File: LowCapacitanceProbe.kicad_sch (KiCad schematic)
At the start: 39 parts, among them J1 u.Fl, J2 SMA, Q1 BF998, U2 SPX3819M5-L-5-0

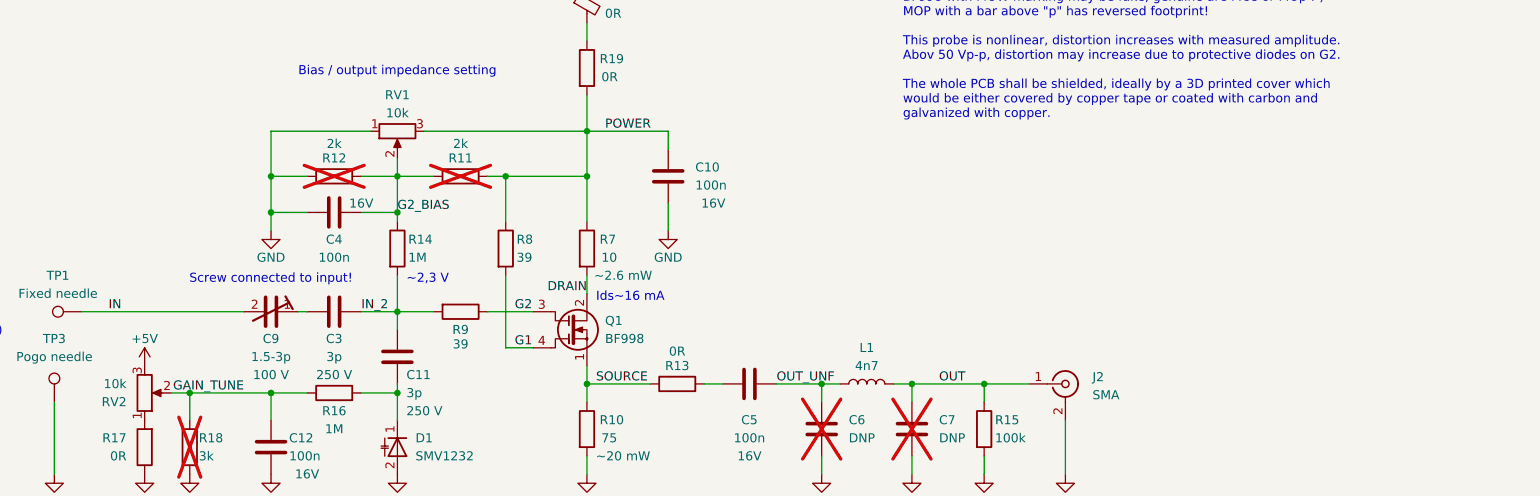
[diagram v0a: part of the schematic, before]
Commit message: Slight fixes, simulation modified for varicap analysis and noise analysis, started routing of PCB.
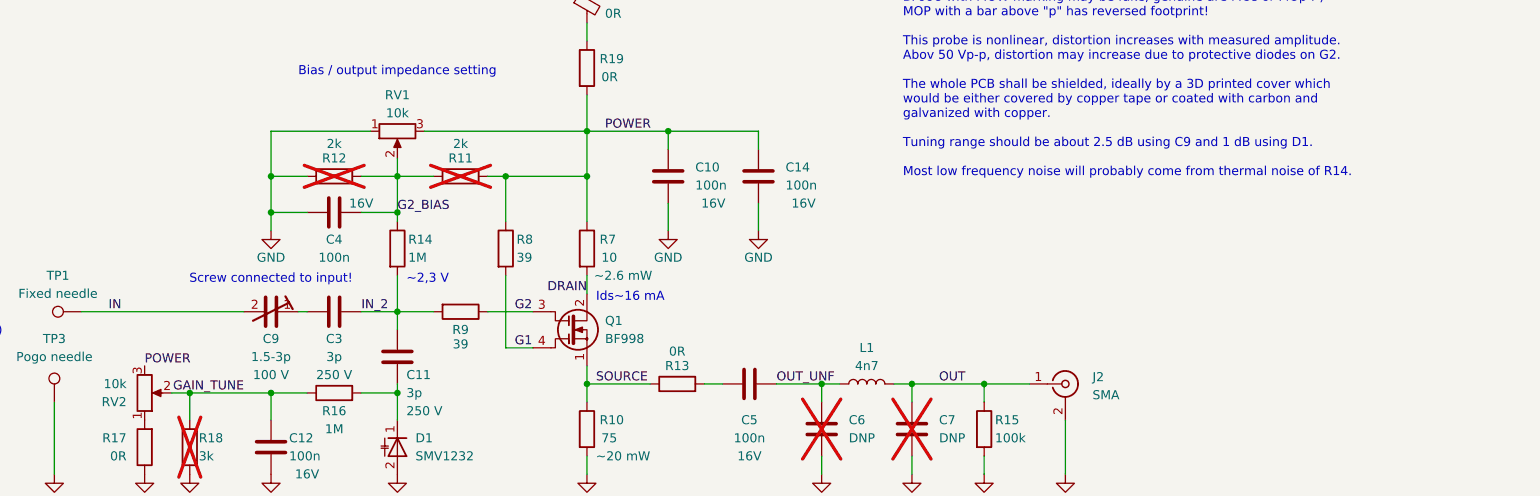
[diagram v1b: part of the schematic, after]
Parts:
- added C14: 100n, Capacitor_SMD:C_0402_1005Metric_Pad0.74x0.62mm_HandSolder, symbol Device:C
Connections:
- net +5V: no longer RV2.3
- net GND: now also C14.1
- net POWER: now also RV2.3, C14.2
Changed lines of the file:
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@@
 		)
 	)
-	(text "Calibration process:\n1) Perform this calibration in ESD safe environment!\n   Short the input, power up the probe (with VNA disconnected).\n   Not shorting the input may affect the measurement.\n2) Connect VNA, measure output impedance of the probe.\n   Tune the bias on gate 2 to get 50 Ohm output.\n3) Disconnect VNA, reconnect it to measure S21 of the probe.\n   (If varicap tuning is assembled, set it to highest possible voltage.)\n   Tune the input capacitor to get 10:1 (-20 dB) response.\n4) (If assembled, use the varicap tuning to fine-tune the gain).\n   If varicap tuning is not used, change bias to fine-tune gain.\n5) Re-measure the output impedance. If out of spec, repeat these steps.\n   This is needed because the parameters are not fully independent.\n   \nNotes:\n1) If desired gain cannot be achieved, change C3.\n2) If output impedance cannot be achieved, change R10.\n3) If varicap tuning is too narrow/broad, change C11.\n   Too large C11 or too steep D1 can introduce non-linearity.\n4) R11, R12 and R18 delinearise the trimmers to make tuning easier.\n5) Trimmer C9 has screw connected to input to make tuning easier.\n   (The input is low impedance source, net after the capacitor is not.)\n6) For tuning C9, use low capacitance isolated tuning screwdriver.\n   Never tune the probe when connected to dangerous voltages!\n7) In case of bad low bandwidth, change L1.\n8) In case of instability, notches and peaks at > 500 MHz, change R7-9.\n9) Clockwise rotation of trimmers increases gain / drain current.\n\nCritical components have MPNs assigned, except for BF998 (look on eBay).\nBF998 with MOW marking may be fake, genuine are MOs or MOp :-)\nMOP with a bar above \"p\" has reversed footprint!\n\nThis probe is nonlinear, distortion increases with measured amplitude.\nAbov 50 Vp-p, distortion may increase due to protective diodes on G2.\n\nThe whole PCB shall be shielded, ideally by a 3D printed cover which\nwould be either covered by copper tape or coated with carbon and\ngalvanized with copper."
+	(text "Calibration process:\n1) Perform this calibration in ESD safe environment!\n   Short the input, power up the probe (with VNA disconnected).\n   Not shorting the input may affect the measurement.\n2) Connect VNA, measure output impedance of the probe.\n   Tune the bias on gate 2 to get 50 Ohm output.\n3) Disconnect VNA, reconnect it to measure S21 of the probe.\n   (If varicap tuning is assembled, set it to highest possible voltage.)\n   Tune the input capacitor to get 10:1 (-20 dB) response.\n4) (If assembled, use the varicap tuning to fine-tune the gain).\n   If varicap tuning is not used, change bias to fine-tune gain.\n5) Re-measure the output impedance. If out of spec, repeat these steps.\n   This is needed because the parameters are not fully independent.\n   \nNotes:\n1) If desired gain cannot be achieved, change C3.\n2) If output impedance cannot be achieved, change R10.\n3) If varicap tuning is too narrow/broad, change C11.\n   Too large C11 or too steep D1 can introduce non-linearity.\n4) R11, R12 and R18 delinearise the trimmers to make tuning easier.\n5) Trimmer C9 has screw connected to input to make tuning easier.\n   (The input is low impedance source, net after the capacitor is not.)\n6) For tuning C9, use low capacitance isolated tuning screwdriver.\n   Never tune the probe when connected to dangerous voltages!\n7) In case of bad low bandwidth, change L1.\n8) In case of instability, notches and peaks at > 500 MHz, change R7-9.\n9) Clockwise rotation of trimmers increases gain / drain current.\n\nCritical components have MPNs assigned, except for BF998 (look on eBay).\nBF998 with MOW marking may be fake, genuine are MOs or MOp :-)\nMOP with a bar above \"p\" has reversed footprint!\n\nThis probe is nonlinear, distortion increases with measured amplitude.\nAbov 50 Vp-p, distortion may increase due to protective diodes on G2.\n\nThe whole PCB shall be shielded, ideally by a 3D printed cover which\nwould be either covered by copper tape or coated with carbon and\ngalvanized with copper.\n\nTuning range should be about 2.5 dB using C9 and 1 dB using D1.\n\nMost low frequency noise will probably come from thermal noise of R14."
 		(exclude_from_sim no)
 		(at 209.55 13.97 0)
@@
 	)
 	(junction
+		(at 176.53 92.71)
+		(diameter 0)
+		(color 0 0 0 0)
+	)
+	(junction
 		(at 210.82 128.27)
 		(diameter 0)
@@
 	(wire
 		(pts
+			(xy 189.23 102.87) (xy 189.23 106.68)
+		)
+		(stroke
+			(width 0)
+			(type default)
+		)
+	)
+	(wire
+		(pts
 			(xy 165.1 77.47) (xy 165.1 80.01)
 		)
@@
 	(wire
 		(pts
+			(xy 176.53 92.71) (xy 189.23 92.71)
+		)
+		(stroke
+			(width 0)
+			(type default)
+		)
+	)
+	(wire
+		(pts
 			(xy 165.1 58.42) (xy 151.13 58.42)
 		)
@@
 	(wire
 		(pts
+			(xy 189.23 95.25) (xy 189.23 92.71)
+		)
+		(stroke
+			(width 0)
+			(type default)
+		)
+	)
+	(wire
+		(pts
 			(xy 109.22 129.54) (xy 120.65 129.54)
 		)
@@
 		)
 	)
+	(label "POWER"
+		(at 102.87 125.73 0)
+		(effects
+			(font
+				(size 1.27 1.27)
+			)
+			(justify left bottom)
+		)
+	)
 	(label "+5V"
 		(at 128.27 58.42 0)
@@
 	)
 	(symbol
+		(lib_id "power:GND")
+		(at 189.23 106.68 0)
+		(unit 1)
+		(exclude_from_sim no)
+		(in_bom yes)
+		(on_board yes)
+		(dnp no)
+		(property "Reference" "#PWR0116"
+			(at 189.23 113.03 0)
+			(effects
+				(font
+					(size 1.27 1.27)
+				)
+				(hide yes)
+			)
+		)
+		(property "Value" "GND"
+			(at 189.23 110.49 0)
+			(effects
+				(font
+					(size 1.27 1.27)
+				)
+			)
+		)
+		(property "Footprint" ""
+			(at 189.23 106.68 0)
+			(effects
+				(font
+					(size 1.27 1.27)
+				)
+				(hide yes)
+			)
+		)
+		(property "Datasheet" ""
+			(at 189.23 106.68 0)
+			(effects
+				(font
+					(size 1.27 1.27)
+				)
+				(hide yes)
+			)
+		)
+		(property "Description" ""
+			(at 189.23 106.68 0)
+			(effects
+				(font
+					(size 1.27 1.27)
+				)
+				(hide yes)
+			)
+		)
+		(pin "1"
+		)
+		(instances
+			(project "LowCapacitanceProbe"
+				(path "/e63e39d7-6ac0-4ffd-8aa3-1841a4541b55"
+					(reference "#PWR0116")
+					(unit 1)
+				)
+			)
+		)
+	)
+	(symbol
 		(lib_id "power:+5V")
 		(at 124.46 55.88 0)
@@
 	)
 	(symbol
+		(lib_id "Device:C")
+		(at 189.23 99.06 180)
+		(unit 1)
+		(exclude_from_sim no)
+		(in_bom yes)
+		(on_board yes)
+		(dnp no)
+		(property "Reference" "C14"
+			(at 193.04 97.7899 0)
+			(effects
+				(font
+					(size 1.27 1.27)
+				)
+				(justify right)
+			)
+		)
+		(property "Value" "100n"
+			(at 193.04 100.33 0)
+			(effects
+				(font
+					(size 1.27 1.27)
+				)
+				(justify right)
+			)
+		)
+		(property "Footprint" "Capacitor_SMD:C_0402_1005Metric_Pad0.74x0.62mm_HandSolder"
+			(at 188.2648 95.25 0)
+			(effects
+				(font
+					(size 1.27 1.27)
+				)
+				(hide yes)
+			)
+		)
+		(property "Datasheet" "https://cz.mouser.com/datasheet/2/40/530l-3169674.pdf"
+			(at 189.23 99.06 0)
+			(effects
+				(font
+					(size 1.27 1.27)
+				)
+				(hide yes)
+			)
+		)
+		(property "Description" "Unpolarized capacitor"
+			(at 189.23 99.06 0)
+			(effects
+				(font
+					(size 1.27 1.27)
+				)
+				(hide yes)
+			)
+		)
+		(property "MPN" "530L104KT16T"
+			(at 189.23 99.06 0)
+			(effects
+				(font
+					(size 1.27 1.27)
+				)
+				(hide yes)
+			)
+		)
+		(property "Mouser" "581-530L104KT16T"
+			(at 189.23 99.06 0)
+			(effects
+				(font
+					(size 1.27 1.27)
+				)
+				(hide yes)
+			)
+		)
+		(property "Rating" "16V"
+			(at 195.58 102.87 0)
+			(effects
+				(font
+					(size 1.27 1.27)
+				)
+			)
+		)
+		(pin "1"
+		)
+		(pin "2"
+		)
+		(instances
+			(project "LowCapacitanceProbe"
+				(path "/e63e39d7-6ac0-4ffd-8aa3-1841a4541b55"
+					(reference "C14")
+					(unit 1)
+				)
+			)
+		)
+	)
+	(symbol
 		(lib_id "power:GND")
 		(at 109.22 140.97 0)
@@
 					(unit 1)
 				)
-			)
-		)
-	)
-	(symbol
-		(lib_id "power:+5V")
-		(at 102.87 125.73 0)
-		(unit 1)
-		(exclude_from_sim no)
-		(in_bom yes)
-		(on_board yes)
-		(dnp no)
-		(property "Reference" "#PWR09"
-			(at 102.87 129.54 0)
-			(effects
-				(font
-					(size 1.27 1.27)
-				)
-				(hide yes)
-			)
-		)
-		(property "Value" "+5V"
-			(at 102.87 121.92 0)
-			(effects
-				(font
-					(size 1.27 1.27)
-				)
-			)
-		)
-		(property "Footprint" ""
-			(at 102.87 125.73 0)
-			(effects
-				(font
-					(size 1.27 1.27)
-				)
-				(hide yes)
-			)
-		)
-		(property "Datasheet" ""
-			(at 102.87 125.73 0)
-			(effects
-				(font
-					(size 1.27 1.27)
-				)
-				(hide yes)
-			)
-		)
-		(property "Description" "Power symbol creates a global label with name \"+5V\""
-			(at 102.87 125.73 0)
-			(effects
-				(font
-					(size 1.27 1.27)
-				)
-				(hide yes)
-			)
-		)
-		(pin "1"
-		)
-		(instances
-			(project "LowCapacitanceProbe"
-				(path "/e63e39d7-6ac0-4ffd-8aa3-1841a4541b55"
-					(reference "#PWR09")
-					(unit 1)
-				)

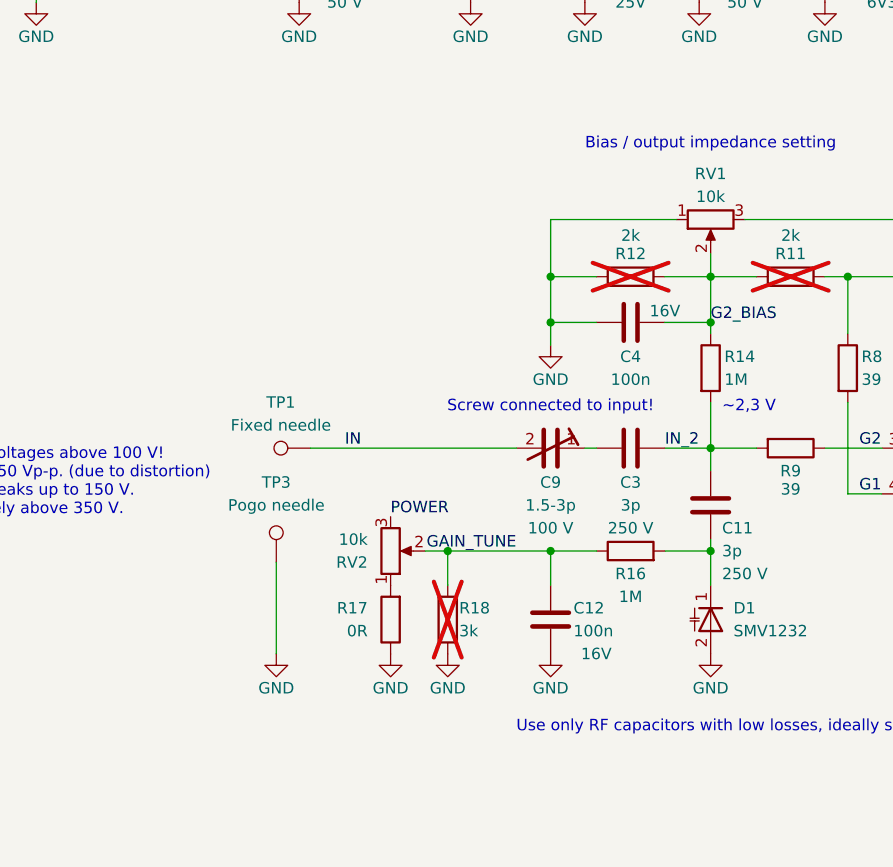
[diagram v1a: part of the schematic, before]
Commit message: Replaced trimmers by smaller SMT types, continued routing.
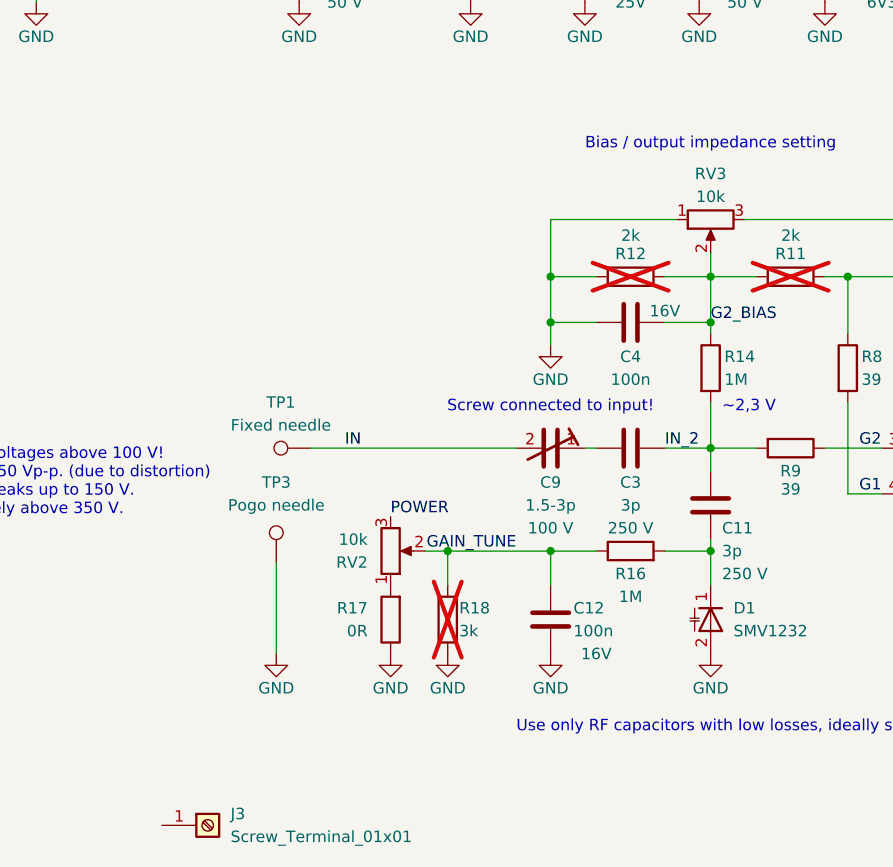
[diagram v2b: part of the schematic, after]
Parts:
- removed RV1: 10k, Potentiometer_THT:Potentiometer_Bourns_3006W_Horizontal, symbol Device:R_Potentiometer
- added J3: Screw_Terminal_01x01, symbol Connector:Screw_Terminal_01x01
- added RV3: 10k, Potentiometer_SMD:Potentiometer_Bourns_3269P_Horizontal, symbol Device:R_Potentiometer
- RV2: footprint Potentiometer_THT:Potentiometer_Bourns_3006W_Horizontal -> Potentiometer_SMD:Potentiometer_Bourns_3269P_Horizontal; MPN Bourns 3006W-1-103 -> 3269P-1-103GLF; Mouser 652-3006W-1-103 -> 652-3269P-1-103GLF
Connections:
- net G2_BIAS: now also RV3.2
- net GND: now also RV3.1
- net POWER: now also RV3.3
